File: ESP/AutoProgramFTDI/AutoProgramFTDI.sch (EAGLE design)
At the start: 21 parts, among them U2 CH340G, U4 74LVC1G08SE, Y1 12MHz

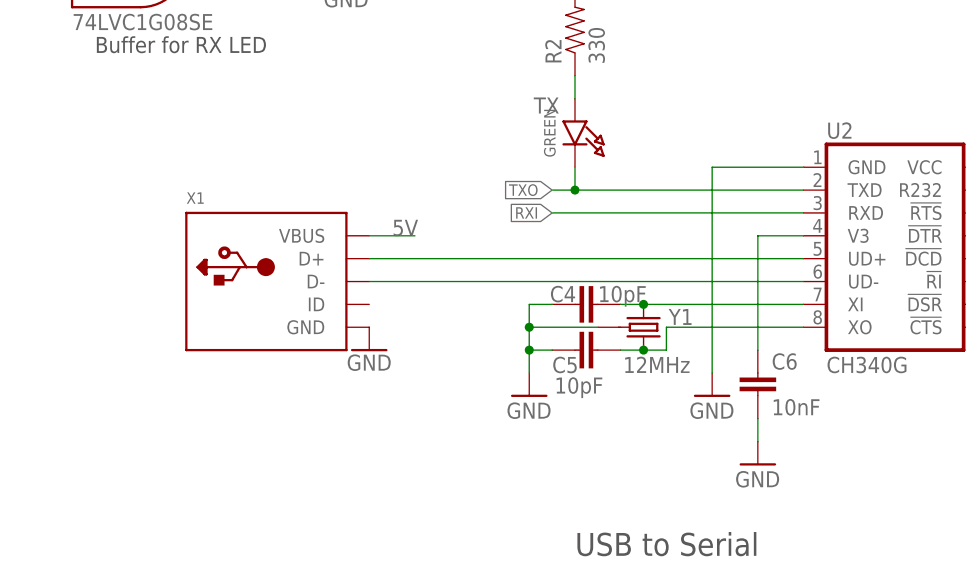
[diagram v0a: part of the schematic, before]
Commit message: update usb & Arduino pro mini
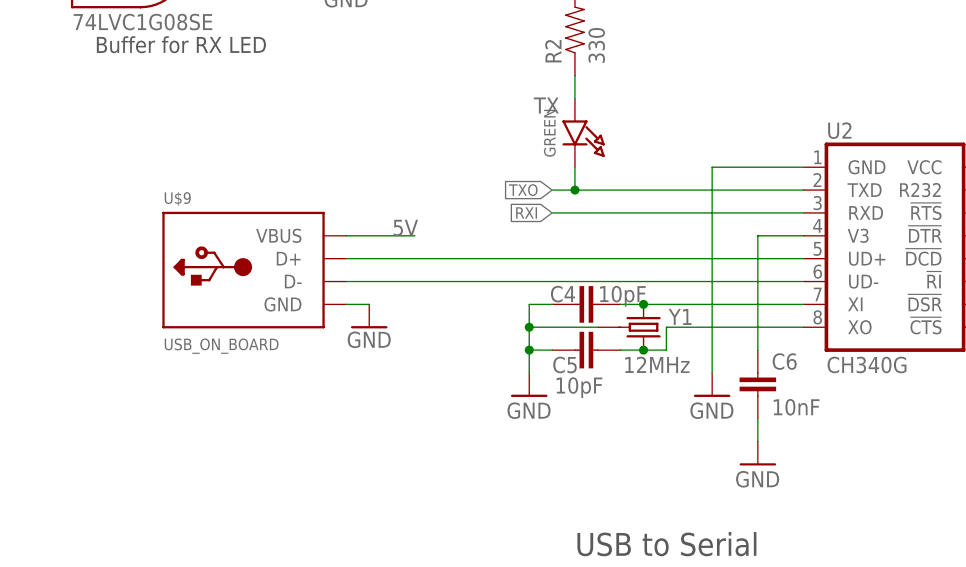
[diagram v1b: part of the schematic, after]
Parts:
- removed X1: (no value), Scott-Connectors:USB_MICRO_20329_V2
- added U$9: USB_ON_BOARD, Scott-Connectors:USB_ON_BOARD
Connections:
- net 5V: now also U$9.VBUS; no longer X1.VBUS
- net GND: now also U$9.GND; no longer X1.GND
- net N$6: now also U$9.D-; no longer X1.D-
- net N$7: now also U$9.D+; no longer X1.D+
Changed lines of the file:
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@@
 <setting verticaltext="up"/>
 </settings>
-<grid distance="0.05" unitdist="inch" unit="inch" style="lines" multiple="1" display="no" altdistance="0.01" altunitdist="inch" altunit="inch"/>
+<grid distance="0.1" unitdist="inch" unit="inch" style="lines" multiple="1" display="no" altdistance="0.01" altunitdist="inch" altunit="inch"/>
 <layers>
 <layer number="1" name="Top" color="4" fill="1" visible="no" active="no"/>
@@
 <part name="GND10" library="SparkFun-Aesthetics" deviceset="GND" device=""/>
 <part name="U4" library="Scott-ICs" deviceset="GATE_74*08" device="" value="74LVC1G08SE"/>
-<part name="X1" library="Scott-Connectors" deviceset="USB" device="_MICRO_20329_V2"/>
 <part name="GND11" library="Scott-Electrical" deviceset="SUPPLY_GND" device=""/>
 <part name="AMS1117" library="Scott-ICs" deviceset="VREG_AMS1117" device="" value="3.3V"/>
@@
 <part name="Q1" library="Scott-Electrical" deviceset="TRANSISTOR_NPN" device="SOT23-3"/>
 <part name="Q2" library="Scott-Electrical" deviceset="TRANSISTOR_NPN" device="SOT23-3"/>
+<part name="U$9" library="Scott-Connectors" deviceset="USB_ON_BOARD" device=""/>
 </parts>
 <sheets>
@@
 <attribute name="VALUE" x="76.2" y="132.08" size="1.778" layer="95" font="vector" rot="R90"/>
 </instance>
-<instance part="X1" gate="G$1" x="63.5" y="91.44">
-<attribute name="NAME" x="53.34" y="100.076" size="1.27" layer="95"/>
-<attribute name="VALUE" x="53.34" y="81.28" size="1.27" layer="96"/>
-</instance>
-<instance part="GND11" gate="1" x="73.66" y="83.82"/>
+<instance part="GND11" gate="1" x="73.66" y="86.36"/>
 <instance part="AMS1117" gate="G$1" x="208.28" y="83.82">
 <attribute name="NAME" x="198.12" y="89.408" size="2.54415" layer="95"/>
@@
 <attribute name="NAME" x="269.24" y="130.81" size="1.778" layer="95" rot="MR180"/>
 <attribute name="VALUE" x="269.24" y="133.35" size="1.778" layer="96" rot="MR180"/>
+</instance>
+<instance part="U$9" gate="1" x="60.96" y="91.44">
+<attribute name="NAME" x="50.8" y="100.076" size="1.27" layer="95"/>
+<attribute name="VALUE" x="50.8" y="83.82" size="1.27" layer="96"/>
 </instance>
 </instances>
@@
 </segment>
 <segment>
-<pinref part="X1" gate="G$1" pin="GND"/>
-<pinref part="GND11" gate="1" pin="GND"/>
-</segment>
-<segment>
 <pinref part="AMS1117" gate="G$1" pin="ADJ/GND"/>
 <pinref part="GND2" gate="1" pin="GND"/>
@@
 <pinref part="GND9" gate="1" pin="GND"/>
 <wire x1="204.47" y1="156.21" x2="204.47" y2="152.4" width="0.1524" layer="91"/>
+</segment>
+<segment>
+<pinref part="U$9" gate="1" pin="GND"/>
+<pinref part="GND11" gate="1" pin="GND"/>
+<wire x1="73.66" y1="88.9" x2="71.12" y2="88.9" width="0.1524" layer="91"/>
 </segment>
 </net>
@@
 <segment>
 <pinref part="U2" gate="U1" pin="UD-"/>
-<wire x1="73.66" y1="91.44" x2="121.92" y2="91.44" width="0.1524" layer="91"/>
-<pinref part="X1" gate="G$1" pin="D-"/>
+<wire x1="71.12" y1="91.44" x2="121.92" y2="91.44" width="0.1524" layer="91"/>
+<pinref part="U$9" gate="1" pin="D-"/>
 </segment>
 </net>
@@
 <segment>
 <pinref part="U2" gate="U1" pin="UD+"/>
-<wire x1="73.66" y1="93.98" x2="121.92" y2="93.98" width="0.1524" layer="91"/>
-<pinref part="X1" gate="G$1" pin="D+"/>
+<wire x1="71.12" y1="93.98" x2="121.92" y2="93.98" width="0.1524" layer="91"/>
+<pinref part="U$9" gate="1" pin="D+"/>
 </segment>
 </net>
@@
 </segment>
 <segment>
-<pinref part="X1" gate="G$1" pin="VBUS"/>
-<wire x1="73.66" y1="96.52" x2="78.74" y2="96.52" width="0.1524" layer="91"/>
+<wire x1="71.12" y1="96.52" x2="78.74" y2="96.52" width="0.1524" layer="91"/>
 <label x="76.2" y="96.52" size="1.778" layer="95"/>
-</segment>
-</net>
+<pinref part="U$9" gate="1" pin="VBUS"/>
+</segment>
+</net>
